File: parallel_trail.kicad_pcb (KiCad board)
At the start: 2 copper layers, 90 x 45 mm, 89 parts, among them U1 TL074, U3 TL074, U4 DG419LDY, U5 TL072, U6 PT2258

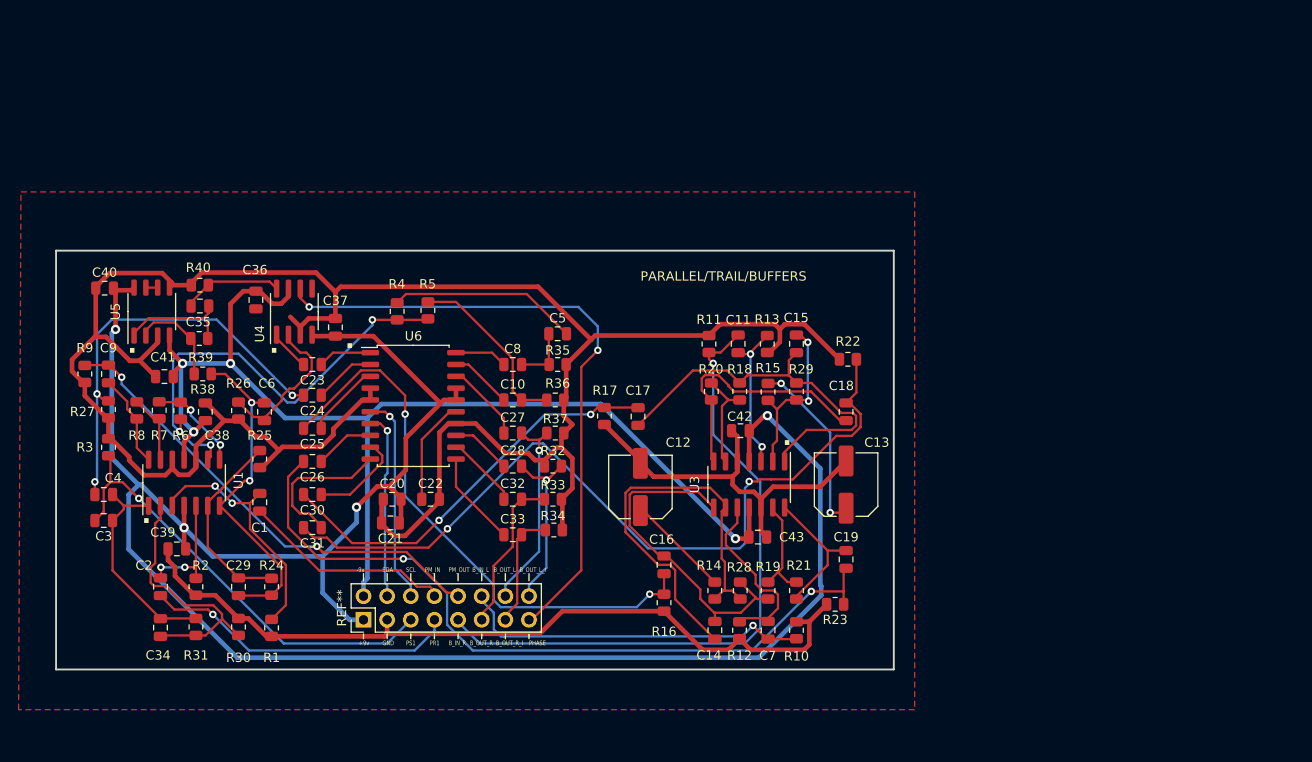
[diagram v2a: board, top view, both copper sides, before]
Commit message: add +5 volt pin
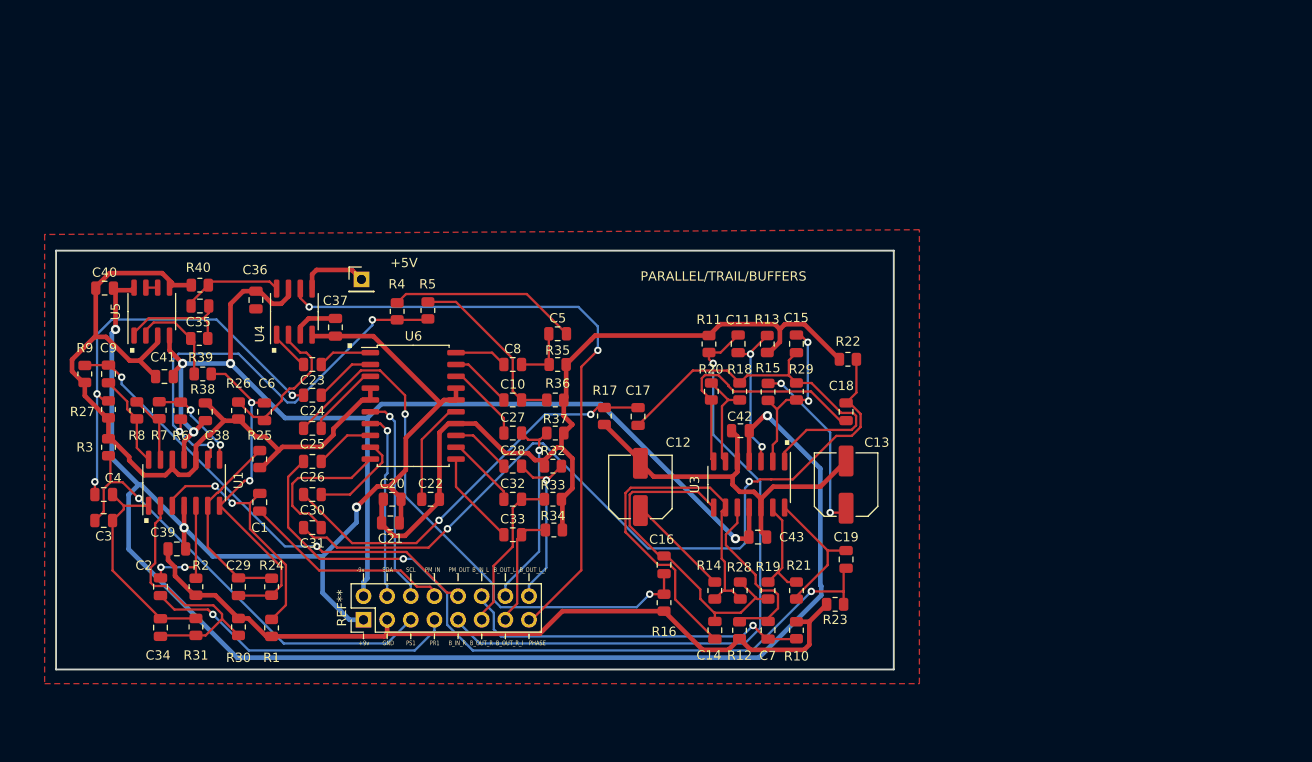
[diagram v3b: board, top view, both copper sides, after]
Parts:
- added +5V: PinHeader_1x01_P2.54mm_Vertical, Connector_PinHeader_2.54mm:PinHeader_1x01_P2.54mm_Vertical, F.Cu at (79.5, 82.5)
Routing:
- net GND: track 364.0 -> 312.5 mm
- net +5V: track 0.00 -> 7.45 mm
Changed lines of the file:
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@@
+    )
+  )
+  (footprint "Connector_PinHeader_2.54mm:PinHeader_1x01_P2.54mm_Vertical" (layer "F.Cu")
+    (at 79.502 82.55)
+    (descr "Through hole straight pin header, 1x01, 2.54mm pitch, single row")
+    (tags "Through hole pin header THT 1x01 2.54mm single row")
+    (attr through_hole)
+    (fp_text reference "+5V" (at 4.572 -1.778) (layer "F.SilkS")
+        (effects (font (size 1 1) (thickness 0.15)))
+    )
+    (fp_text value "PinHeader_1x01_P2.54mm_Vertical" (at 0 2.33) (layer "F.Fab")
+        (effects (font (size 1 1) (thickness 0.15)))
+    )
+    (fp_text user "${REFERENCE}" (at 0 0 90) (layer "F.Fab")
+        (effects (font (size 1 1) (thickness 0.15)))
+    )
+    (fp_line (start -1.33 -1.33) (end 0 -1.33)
+      (stroke (width 0.12) (type solid)) (layer "F.SilkS"))
+    (fp_line (start -1.33 0) (end -1.33 -1.33)
+      (stroke (width 0.12) (type solid)) (layer "F.SilkS"))
+    (fp_line (start -1.33 1.27) (end -1.33 1.33)
+      (stroke (width 0.12) (type solid)) (layer "F.SilkS"))
+    (fp_line (start -1.33 1.27) (end 1.33 1.27)
+      (stroke (width 0.12) (type solid)) (layer "F.SilkS"))
+    (fp_line (start -1.33 1.33) (end 1.33 1.33)
+      (stroke (width 0.12) (type solid)) (layer "F.SilkS"))
+    (fp_line (start 1.33 1.27) (end 1.33 1.33)
+      (stroke (width 0.12) (type solid)) (layer "F.SilkS"))
+    (fp_line (start -1.8 -1.8) (end -1.8 1.8)
+      (stroke (width 0.05) (type solid)) (layer "F.CrtYd"))
+    (fp_line (start -1.8 1.8) (end 1.8 1.8)
+      (stroke (width 0.05) (type solid)) (layer "F.CrtYd"))
+    (fp_line (start 1.8 -1.8) (end -1.8 -1.8)
+      (stroke (width 0.05) (type solid)) (layer "F.CrtYd"))
+    (fp_line (start 1.8 1.8) (end 1.8 -1.8)
+      (stroke (width 0.05) (type solid)) (layer "F.CrtYd"))
+    (fp_line (start -1.27 -0.635) (end -0.635 -1.27)
+      (stroke (width 0.1) (type solid)) (layer "F.Fab"))
+    (fp_line (start -1.27 1.27) (end -1.27 -0.635)
+      (stroke (width 0.1) (type solid)) (layer "F.Fab"))
+    (fp_line (start -0.635 -1.27) (end 1.27 -1.27)
+      (stroke (width 0.1) (type solid)) (layer "F.Fab"))
+    (fp_line (start 1.27 -1.27) (end 1.27 1.27)
+      (stroke (width 0.1) (type solid)) (layer "F.Fab"))
+    (fp_line (start 1.27 1.27) (end -1.27 1.27)
+      (stroke (width 0.1) (type solid)) (layer "F.Fab"))
+    (pad "1" thru_hole rect (at 0 0) (size 1.7 1.7) (drill 1) (layers "*.Cu" "*.Mask")
+      (net 64 "+5V"))
+    (model "${KICAD6_3DMODEL_DIR}/Connector_PinHeader_2.54mm.3dshapes/PinHeader_1x01_P2.54mm_Vertical.wrl"
+      (offset (xyz 0 0 0))
+      (scale (xyz 1 1 1))
+      (rotate (xyz 0 0 0))
     )
   )
@@
   (gr_line (start 89.8848 114.9302) (end 89.8848 114.1682)
     (stroke (width 0.15) (type default)) (layer "F.SilkS"))
-  (gr_rect (start 136.694 124.46) (end 46.694 79.46)
+  (gr_rect (start 46.694 79.46) (end 136.694 124.46)
     (stroke (width 0.2) (type default)) (fill none) (layer "Edge.Cuts"))
   (gr_text "." (at 54.356 90.678) (layer "F.SilkS")
@@
   (segment (start 100.9975 100.6202) (end 100.5126 100.6202) (width 0.5) (layer "F.Cu") (net 22))
   (segment (start 101.092 118.1945) (end 98.661 120.6255) (width 0.5) (layer "F.Cu") (net 22))
-  (segment (start 98.4935 83.3414) (end 77.2688 83.3414) (width 0.5) (layer "F.Cu") (net 22))
   (segment (start 81.666 106.36) (end 81.666 108.712) (width 0.5) (layer "F.Cu") (net 22))
   (segment (start 55.6813 91.2812) (end 57.39 92.99) (width 0.5) (layer "F.Cu") (net 22))
@@
   (segment (start 59.1495 82.9322) (end 59.1495 83.17) (width 0.5) (layer "F.Cu") (net 22))
   (segment (start 68.7963 102.7665) (end 70.6391 100.9237) (width 0.5) (layer "F.Cu") (net 22))
-  (segment (start 62.3559 81.8158) (end 74.6216 81.8158) (width 0.5) (layer "F.Cu") (net 22))
   (segment (start 49.784 93.6225) (end 49.6047 93.6225) (width 0.5) (layer "F.Cu") (net 22))
   (segment (start 57.6145 89.348) (end 55.6813 91.2812) (width 0.5) (layer "F.Cu") (net 22))
@@
   (segment (start 71.0178 100.545) (end 75.1978 100.545) (width 0.5) (layer "F.Cu") (net 22))
   (segment (start 61.722 101.919) (end 61.722 102.7731) (width 0.5) (layer "F.Cu") (net 22))
-  (segment (start 77.2688 83.3414) (end 76.708 83.9022) (width 0.5) (layer "F.Cu") (net 22))
   (segment (start 62.8451 95.824) (end 62.738 95.824) (width 0.5) (layer "F.Cu") (net 22))
   (segment (start 101.092 106.2755) (end 101.092 109.474) (width 0.5) (layer "F.Cu") (net 22))
@@
   (segment (start 109.474 102.0105) (end 109.474 102.3125) (width 0.5) (layer "F.Cu") (net 22))
   (segment (start 52.324 99.6715) (end 52.324 97.4325) (width 0.5) (layer "F.Cu") (net 22))
-  (segment (start 74.6216 81.8158) (end 76.708 83.9022) (width 0.5) (layer "F.Cu") (net 22))
   (segment (start 58.724 112.72) (end 58.724 111.506) (width 0.5) (layer "F.Cu") (net 22))
   (segment (start 75.1978 100.545) (end 76.4874 99.2554) (width 0.5) (layer "F.Cu") (net 22))
@@
   (segment (start 97.3977 101.2119) (end 98.1551 101.9693) (width 0.5) (layer "F.Cu") (net 22))
   (segment (start 55.6813 91.2812) (end 55.6812 91.2813) (width 0.5) (layer "F.Cu") (net 22))
-  (segment (start 76.708 83.9022) (end 76.708 86.746) (width 0.5) (layer "F.Cu") (net 22))
   (segment (start 69.2771 120.904) (end 67.3486 118.9755) (width 0.5) (layer "F.Cu") (net 22))
   (segment (start 127.0926 87.3711) (end 124.9916 87.3711) (width 0.5) (layer "F.Cu") (net 22))
@@
   (segment (start 118.9324 122.3484) (end 120.1228 121.158) (width 0.5) (layer "F.Cu") (net 22))
   (segment (start 49.784 95.0567) (end 52.1598 97.4325) (width 0.5) (layer "F.Cu") (net 22))
-  (segment (start 61.227 83.17) (end 61.227 82.9447) (width 0.5) (layer "F.Cu") (net 22))
   (segment (start 123.7347 104.8196) (end 128.8109 104.8196) (width 0.5) (layer "F.Cu") (net 22))
   (segment (start 100.5126 100.6202) (end 99.1635 101.9693) (width 0.5) (layer "F.Cu") (net 22))
-  (segment (start 104.1713 89.0192) (end 98.4935 83.3414) (width 0.5) (layer "F.Cu") (net 22))
   (segment (start 105.606 98.1425) (end 109.474 102.0105) (width 0.5) (layer "F.Cu") (net 22))
   (segment (start 122.428 106.1263) (end 122.428 107.058) (width 0.5) (layer "F.Cu") (net 22))
   (segment (start 68.2002 99.4587) (end 69.1741 99.4587) (width 0.5) (layer "F.Cu") (net 22))
-  (segment (start 72.933 87.6478) (end 71.8612 86.576) (width 0.5) (layer "F.Cu") (net 22))
   (segment (start 55.6812 91.2813) (end 54.6096 91.2813) (width 0.5) (layer "F.Cu") (net 22))
   (segment (start 100.9885 106.172) (end 102.1684 104.9921) (width 0.5) (layer "F.Cu") (net 22))
@@
   (segment (start 54.551 101.6186) (end 54.551 101.9866) (width 0.5) (layer "F.Cu") (net 22))
   (segment (start 89.662 98.044) (end 88.8471 98.044) (width 0.5) (layer "F.Cu") (net 22))
-  (segment (start 61.227 82.9447) (end 62.3559 81.8158) (width 0.5) (layer "F.Cu") (net 22))
   (segment (start 104.609 88.5815) (end 104.1713 89.0192) (width 0.5) (layer "F.Cu") (net 22))
   (segment (start 87.884 106.4027) (end 84.1829 110.1038) (width 0.5) (layer "F.Cu") (net 22))
@@
   (segment (start 56.3445 88.0072) (end 56.3445 88.585) (width 0.25) (layer "F.Cu") (net 63))
   (segment (start 61.5375 89.2705) (end 61.167 88.9) (width 0.25) (layer "F.Cu") (net 63))
+  (segment (start 78.486 81.534) (end 79.502 82.55) (width 0.5) (layer "F.Cu") (net 64))
+  (segment (start 74.203 83.541) (end 74.203 82.007) (width 0.5) (layer "F.Cu") (net 64))
+  (segment (start 74.676 81.534) (end 78.486 81.534) (width 0.5) (layer "F.Cu") (net 64))
+  (segment (start 74.203 82.007) (end 74.676 81.534) (width 0.5) (layer "F.Cu") (net 64))
   (segment (start 97.7948 119.1212) (end 103.124 113.792) (width 0.25) (layer "F.Cu") (net 65))
   (segment (start 103.124 113.792) (end 103.124 91.948) (width 0.25) (layer "F.Cu") (net 65))
@@
     (polygon
       (pts
-        (xy 42.926 73.152)
-        (xy 138.938 73.152)
-        (xy 138.938 128.778)
-        (xy 42.672 128.778)
+        (xy 45.466 77.724)
+        (xy 45.466 125.984)
+        (xy 139.446 125.984)
+        (xy 139.446 77.216)
       )
     )
